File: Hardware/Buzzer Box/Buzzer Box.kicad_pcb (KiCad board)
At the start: 2 copper layers, 185 x 65 mm, 97 parts, among them IC1 4691, IC10 4691, IC11 4691, IC12 4691, IC2 4691, IC3 4691, IC4 4691, IC5 4691, IC6 4691, IC7 4691, IC8 4691, IC9 4691, J1 GPIO 39, J11 USB_C_Receptacle_USB2.0_16P, J13 NC3FAAH, J14 NC3FAAH, J17 NC3FAAH, J18 NC3FAAH, J19 GND, J2 JTAG, J20 3V3, J21 24v, J22 5V, J23 NC3FAAH, J24 NC3FAAH, J25 NC3FAAH, J26 NC3FAAH, J4 GPIO 39, J5 GPIO 39, J6 UART, Q1 AO3400A, Q2 AO3400A, Q3 AO3400A, Q4 AO3400A, Q5 AO3400A, Q6 AO3400A, Q7 AO3400A, Q8 AO3400A, U1 LTV-817S, U10 ESP32-S3-WROOM-1, U2 USBLC6-2SC6, U3 LTV-817S, U4 LTV-817S, U5 LTV-817S, U6 LTV-817S, U7 LTV-817S, U8 LTV-817S, U9 LTV-817S

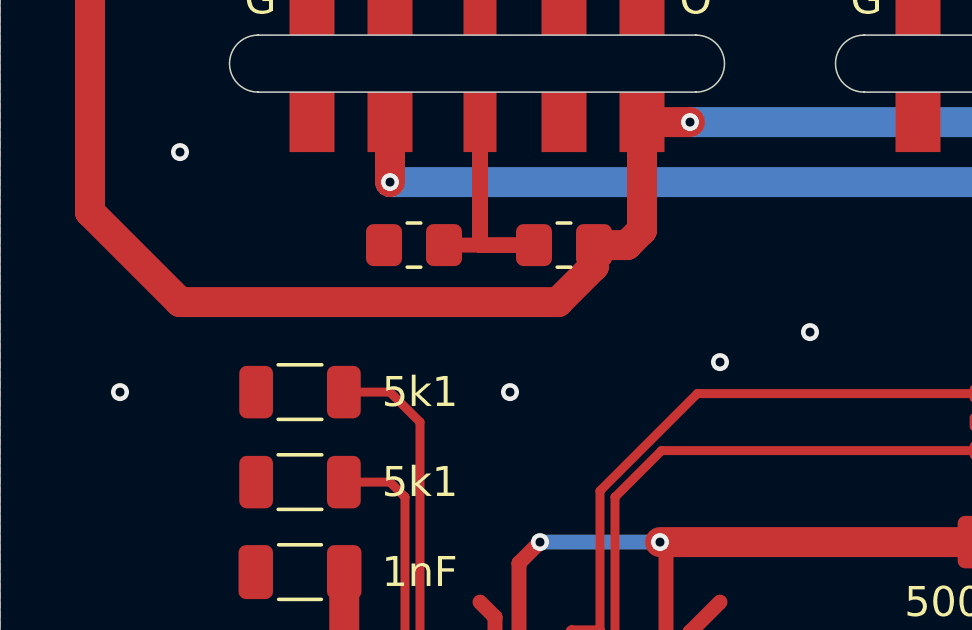
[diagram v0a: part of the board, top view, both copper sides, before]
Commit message: Upgrade zu .net9
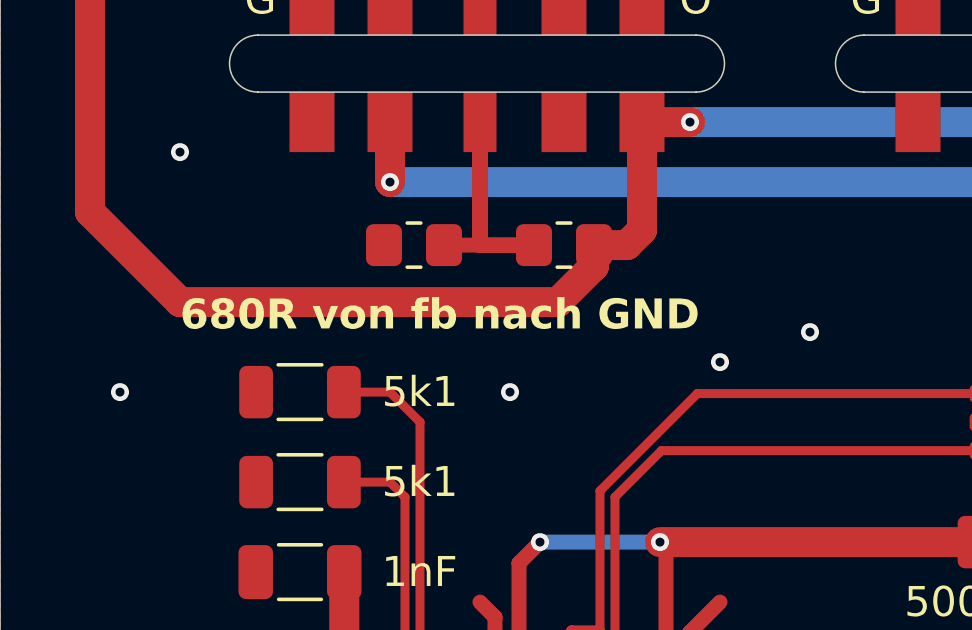
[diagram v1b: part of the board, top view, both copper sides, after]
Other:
- board text added: "680R von fb nach GND"
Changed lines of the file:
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@@
+		)
+	)
+	(gr_text "680R von fb nach GND"
+		(at 49 105 0)
+		(layer "F.SilkS")
+		(effects
+			(font
+				(size 1 1)
+				(thickness 0.25)
+				(bold yes)
+			)
+			(justify left bottom)
 		)
 	)
